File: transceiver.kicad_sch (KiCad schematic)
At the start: 82 parts, among them J2 Conn_01x04_Male, J3 Conn_01x04_Male, J4 Conn_01x04_Male, J5 Conn_01x06_Male, J6 Conn_01x05_Male, J7 Conn_01x05_Male, J8 Conn_01x05_Male, J9 Conn_01x04_Male, U10 74LVC1G3157, U11 SP330EEY-L, U12 TXS0104EDR, U13 74LVC1G3157, U14 MAX3222EIPW, U4 74LVC1G3157, U5 SP330EEY-L, U6 74LVC1G3157, U7 TLV75525PDBV, U8 TXS0104EDR, U9 TLV75518PDBV

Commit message: After update to kicak 9.0
Signed-off-by: Marc Kelly <mpkelly@achenar.co.uk>
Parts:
- C19, C20, C21, C22, C23, C24, C25, C26, C27, C28, C29, C30, C31, C32, C33, C34, C35, C36, C37, C38, C39: MFN (none) -> Kemet; MFP (none) -> C0603C104J4RACTU; SUPPLIER (none) -> Mouser; SUPPLIER_LINK (none) -> https://www.mouser.co.uk/ProductDetail/KEMET/C0603C104J4RAC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; SUPPLIER_PN (none) -> 80-C0603C104J4R
- D10, D11, D4, D5, D6, D7, D8, D9: MFN (none) -> Wurth; MFP (none) -> 155060GS75300; SUPPLIER (none) -> Mouser; SUPPLIER_LINK (none) -> https://www.mouser.co.uk/ProductDetail/Wurth-Elektronik/155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; SUPPLIER_PN (none) -> 710-155060GS75300
- J2, J3, J4, J9: MFN (none) -> Ampheonol; MFP (none) -> 68604-804HLF; SUPPLIER (none) -> Mouser; SUPPLIER_LINK (none) -> https://www.mouser.co.uk/ProductDetail/Amphenol-FCI/68604-8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; SUPPLIER_PN (none) -> 649-68604-804HLF
- J5: MFN (none) -> Ampheonol; MFP (none) -> 68024-106HLF; SUPPLIER (none) -> Mouser; SUPPLIER_LINK (none) -> https://www.mouser.co.uk/ProductDetail/Amphenol-FCI/68024-1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; SUPPLIER_PN (none) -> 649-68024-106HLF
- J6, J7, J8: MFN (none) -> Ampheonol; MFP (none) -> 68024-405HLF; SUPPLIER (none) -> Mouser; SUPPLIER_LINK (none) -> https://www.mouser.co.uk/ProductDetail/Amphenol-FCI/68024-4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; SUPPLIER_PN (none) -> 649-68024-405HLF
- JP1, JP12: MFN (none) -> Ampheonol; MFP (none) -> 57202-F52-03LF; SUPPLIER (none) -> Mouser; SUPPLIER_LINK (none) -> https://www.mouser.co.uk/ProductDetail/Amphenol-FCI/57202-F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; SUPPLIER_PN (none) -> 649-57202-F52-03LF
- JP19, JP23, JP4, JP8: MFN (none) -> Ampheonol; MFP (none) -> 57202-G52-04LF; SUPPLIER (none) -> Mouser; SUPPLIER_LINK (none) -> https://www.mouser.co.uk/ProductDetail/Amphenol-FCI/57202-G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; SUPPLIER_PN (none) -> 649-57202-G52-04LF
- JP27, JP28, JP29, JP30: MFN (none) -> Samtech; MFP (none) -> TMM-116-01-G-S-SM; Notes (none) -> Buy a strip, cut to length! get a x16; SUPPLIER (none) -> Mouser; SUPPLIER_LINK (none) -> https://www.mouser.co.uk/ProductDetail/Samtec/TMM-116-01-G-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; SUPPLIER_PN (none) -> 200-TMM11601GSSM
- R10, R11, R12, R13, R14, R9: value 4.7k -> 4k7; MFN (none) -> Generic; SUPPLIER (none) -> Mouser; SUPPLIER_PN (none) -> 603-RT0603DRE074K7L
- R15, R16, R17, R18, R19: MFN (none) -> Generic; SUPPLIER (none) -> Mouser; SUPPLIER_PN (none) -> 603-RT0603DRE074K7L
- R21, R22, R23, R24, R25, R26, R27, R28: MFN (none) -> Generic; SUPPLIER (none) -> Mouser; SUPPLIER_PN (none) -> 754-RG1608P-331-BT5
- R31, R32, R33, R34: MFN (none) -> Generic; SUPPLIER (none) -> Mouser; SUPPLIER_PN (none) -> 603-RT0603FRE07120RL
- U10, U13, U4, U6: MFN (none) -> TI; MFP (none) -> SN74LVC1G3157DBVR; SUPPLIER (none) -> Mouser; SUPPLIER_LINK (none) -> https://www.mouser.co.uk/ProductDetail/Texas-Instruments/SN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; SUPPLIER_PN (none) -> 595-SN74LVC1G3157DBV
- U11, U5: MFN (none) -> MaxLinear; MFP (none) -> SP330EEY-L; SUPPLIER (none) -> Mouser; SUPPLIER_LINK (none) -> https://www.mouser.co.uk/ProductDetail/MaxLinear/SP330EEY-L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; SUPPLIER_PN (none) -> 701-SP330EEY-L
- U12, U8: MFN (none) -> TI; MFP (none) -> TXS0104ED; SUPPLIER (none) -> Mouser; SUPPLIER_LINK (none) -> https://www.mouser.co.uk/ProductDetail/Texas-Instruments/TX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; SUPPLIER_PN (none) -> 595-TXS0104ED
- U14: MFN (none) -> TI; MFP (none) -> MAX3222ECDWR; SUPPLIER (none) -> Mouser; SUPPLIER_LINK (none) -> https://www.mouser.co.uk/ProductDetail/Texas-Instruments/MA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; SUPPLIER_PN (none) -> 595-MAX3222ECDWR
- U7: MFN (none) -> TI; MFP (none) -> TLV75525PDBVR; SUPPLIER (none) -> Mouser; SUPPLIER_LINK (none) -> https://www.mouser.co.uk/ProductDetail/Texas-Instruments/TL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; SUPPLIER_PN (none) -> 595-TLV75525PDBVR
- U9: MFN (none) -> TI; MFP (none) -> TLV75518PDBVR; SUPPLIER (none) -> Mouser; SUPPLIER_LINK (none) -> https://www.mouser.co.uk/ProductDetail/Texas-Instruments/TL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; SUPPLIER_PN (none) -> 595-TLV75518PDBVR

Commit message: Updated to remove the level shifters
Just have 3v3 ttl outputs for now, trancievers will be on different
boards
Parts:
- removed C19, C20, C21, C22, C23, C24, C25, C26, C27, C28, C29, C30, C31, C32, C33, C34, C35, C36, C37, C38, C39: 100nF, Capacitor_SMD:C_0603_1608Metric_Pad1.08x0.95mm_HandSolder, symbol Device:C_Small
- removed J2, J3, J4, J9: Conn_01x04_Male, Connector_PinHeader_2.54mm:PinHeader_1x04_P2.54mm_Vertical, symbol Connector:Conn_01x04_Male
- removed J5: Conn_01x06_Male, Connector_PinHeader_2.54mm:PinHeader_1x06_P2.54mm_Vertical, symbol Connector:Conn_01x06_Male
- removed J6, J7, J8: Conn_01x05_Male, Connector_PinHeader_2.54mm:PinHeader_1x05_P2.54mm_Vertical, symbol Connector:Conn_01x05_Male
- removed JP1, JP12: Jumper, Connector_PinHeader_2.00mm:PinHeader_2x03_P2.00mm_Vertical_SMD, symbol Connector_Generic:Conn_02x03_Odd_Even
- removed JP19, JP23, JP4, JP8: Jumper, Connector_PinHeader_2.00mm:PinHeader_2x04_P2.00mm_Vertical_SMD, symbol Connector_Generic:Conn_02x04_Odd_Even
- removed JP27, JP28, JP29, JP30: Jumper, Connector_PinHeader_2.00mm:PinHeader_1x02_P2.00mm_Vertical_SMD_Pin1Left, symbol Device:Jumper
- removed R10, R11, R12, R13, R14, R15, R18, R19, R9: 4k7, Resistor_SMD:R_0603_1608Metric_Pad0.98x0.95mm_HandSolder, symbol Device:R_Small
- removed R31, R32, R33, R34: 120R, Resistor_SMD:R_0603_1608Metric_Pad0.98x0.95mm_HandSolder, symbol Device:R_Small
- removed U10, U13, U4, U6: 74LVC1G3157, Package_TO_SOT_SMD:SOT-23-6_Handsoldering, symbol 74xGxx:74LVC1G3157
- removed U11, U5: SP330EEY-L, Package_SO:TSSOP-24_4.4x7.8mm_P0.65mm, symbol local:SP330EEY-L
- removed U12, U8: TXS0104EDR, Package_SO:SOIC-14_3.9x8.7mm_P1.27mm, symbol local:TXS0104EDR
- removed U14: MAX3222EIPW, Package_SO:SO-20_12.8x7.5mm_P1.27mm, symbol local:MAX3222EIPW
- added D1, D2, D3, D4: Y_LED, LED_SMD:LED_0603_1608Metric_Pad1.05x0.95mm_HandSolder, symbol Device:LED
- added D18, D19, D20, D21: ESDS304, Package_TO_SOT_SMD:SOT-23-5, symbol Power_Protection:ESDS304
- added J1, J2, J3, J4: Conn_02x06_Odd_Even, symbol Connector_Generic:Conn_02x06_Odd_Even
- added R1, R2, R3, R4: 330R, Resistor_SMD:R_0603_1608Metric_Pad0.98x0.95mm_HandSolder, symbol Device:R_Small
- renumbered D9 to D10, D10 to D11, D11 to D12, D4 to D5, D5 to D6, D6 to D7, D7 to D8, D8 to D9, JP15 to JP1, R26 to R10, R27 to R11, R28 to R12, R16 to R13, R17 to R14, R21 to R5, R22 to R6, R23 to R7, R24 to R8, R25 to R9, U7 to U1, U9 to U2
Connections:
- net BDBUS0 is gone; now on net ADBUS0: R5.2
- net BDBUS1 is gone; now on net ADBUS1: R6.2
- net CDBUS0 is gone; now on net ADBUS0: R7.2
- net CDBUS1 is gone; now on net ADBUS1: R8.2
- net DDBUS0 is gone; now on net ADBUS0: R11.2
- net DDBUS1 is gone; now on net ADBUS1: R12.2
- net Vdrive is gone; now on net GND: JP1.2 (Pin_2), JP1.4 (Pin_4), JP1.6 (Pin_6), JP1.8 (Pin_8)
- net +3V3: no longer JP1.5 (Pin_5)
- net ADBUS0: now also D18.1 (K), J1.1 (Pin_1), J2.1 (Pin_1), J3.1 (Pin_1), J4.1 (Pin_1)
- net ADBUS1: now also D18.3 (K), J1.2 (Pin_2), J2.2 (Pin_2), J3.2 (Pin_2), J4.2 (Pin_2)
- net ADBUS2: now also D18.4 (K), J1.3 (Pin_3), J2.3 (Pin_3), J3.3 (Pin_3), J4.3 (Pin_3)
- net ADBUS3: now also D18.5 (K), J1.4 (Pin_4), J2.4 (Pin_4), J3.4 (Pin_4), J4.4 (Pin_4)
- net ADBUS4: now also J1.5 (Pin_5), J2.5 (Pin_5), J3.5 (Pin_5), J4.5 (Pin_5)
- net ADBUS7: now also J1.6 (Pin_6), J2.6 (Pin_6), J3.6 (Pin_6), J4.6 (Pin_6)
- net CTSn_2: now also D19.5 (K)
- net CTSn_3: now also D20.5 (K)
- net CTSn_4: now also D21.5 (K)
- net GND: now also D18.2 (A), D19.2 (A), D20.2 (A), D21.2 (A), J1.7 (Pin_7), J1.8 (Pin_8), J2.7 (Pin_7), J2.8 (Pin_8), J3.7 (Pin_7), J3.8 (Pin_8), J4.7 (Pin_7), J4.8 (Pin_8)
- net RTSn_2: now also D19.4 (K)
- net RTSn_3: now also D20.4 (K)
- net RTSn_4: now also D21.4 (K)
- net RXD_2: now also D19.3 (K)
- net RXD_3: now also D20.3 (K)
- net RXD_4: now also D21.3 (K)
- net TXD_2: now also D19.1 (K)
- net TXD_3: now also D20.1 (K)
- net TXD_4: now also D21.1 (K)
- net VBUS: now also J1.9 (Pin_9), J2.9 (Pin_9), J3.9 (Pin_9), J4.9 (Pin_9), R1.2
- new net: D1.2 (A), R1.1
- new net: D2.2 (A), R2.1
- new net: D4.2 (A), R4.1
- new net: D3.2 (A), R3.1
- new net 1V8: J1.11 (Pin_11), J2.11 (Pin_11), J3.11 (Pin_11), J4.11 (Pin_11), R4.2
- new net 2V5: J1.10 (Pin_10), J2.10 (Pin_10), J3.10 (Pin_10), J4.10 (Pin_10), R3.2
- new net 3V3: J1.12 (Pin_12), J2.12 (Pin_12), J3.12 (Pin_12), J4.12 (Pin_12), R2.2
- new net 3v3: JP1.5 (Pin_5)
- no-connect marks 14 -> 8
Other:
- note added: "Mapping of Busto Serial 0: TXD 1: RXD 2: RTSn 3: CTSn 4: DTRn 5: DSRn 6: DCDn 7: TXDEN"
- note added: "Ouput Connector 2x6 (10 pin) 1: TXD 2: RXD 3: RTSn 4: CTSn 5: DTRn 6: TXDEN 7: GND 8; GND 9: 5v0 10: 2v5 11: 1v8 12: 3v3"
- note added: "Power Test Point and LEDS"
- note added: "We should use shottkey protection clamps 2x8 arrays maybe"
- note removed: "1.27mm 2pin headers - Disconnect XCVR"
- note removed: "2mm 2pin headers - Disconnect XCVR"
- note removed: "BUSA: CMOS/TTL BUSB: RS232 BUSC: RS422/485/RS232 BUSC: RS422/485/RS232"
- note removed: "Convert the 3v3 Logic to 1v8, then we can do 1v8 to ANY upto 5V on the second stage."
- note removed: "Gives direct TTL access"
- note removed: "Gives direct TTL access 3v3 bypassing level shifters"
- note removed: "Mapping of Bus to Serial 0: TXD 1: RXD 2: RTSn 3: CTSn 4: DTRn 5: DSRn 6: DCDn 7: TXDEN"
- note removed: "Maybe some screw terminals?"
- note removed: "Port 2 - RS232"
- note removed: "Port 3 - RS422/485/RS232"
- note removed: "Port 4 - RS422/485/RS232"
- note removed: "Termination resistors for the rs485 Ports 3 & 4"
- moved on the sheet: D10, D11, D12, D5, D6, D7, D8, D9, JP1, R10, R11, R12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

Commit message: Updated power leds and external protection on Serial
Signed-off-by: Marc Kelly <mpkelly@achenar.co.uk>
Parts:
- removed D3: Y_LED, LED_SMD:LED_0603_1608Metric_Pad1.05x0.95mm_HandSolder, symbol Device:LED
- removed R3: 330R, Resistor_SMD:R_0603_1608Metric_Pad0.98x0.95mm_HandSolder, symbol Device:R_Small
- added D2, D4: ESDS304, Package_TO_SOT_SMD:SOT-23-5, symbol Power_Protection:ESDS304
- added D8: Y_LED, LED_SMD:LED_0603_1608Metric_Pad1.05x0.95mm_HandSolder, symbol Device:LED
- added Q1, Q2: SI500N025UK-TP, Package_TO_SOT_SMD:SOT-23, symbol Transistor_FET:Q_NMOS_GSD
- added R2, R5, R6: 330R, Resistor_SMD:R_0603_1608Metric_Pad0.98x0.95mm_HandSolder, symbol Device:R_Small
- J1, J2, J3, J4: footprint (none) -> Connector_PinSocket_2.54mm:PinSocket_2x06_P2.54mm_Horizontal
- renumbered D18 to D1, D2 to D10, D5 to D11, D6 to D12, D7 to D13, D8 to D14, D9 to D15, D10 to D16, D11 to D17, D12 to D18, D19 to D3, D20 to D5, D21 to D6, D4 to D7, D1 to D9, R4 to R1, R8 to R10, R9 to R11, R10 to R12, R11 to R13, R12 to R14, R13 to R15, R14 to R16, R1 to R3, R2 to R4, R5 to R7, R6 to R8, R7 to R9
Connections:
- net 1V8: no longer R1.2
- net 3v3: now also R1.2, R2.2
- net ADBUS0: no longer J2.1 (Pin_1), J3.1 (Pin_1), J4.1 (Pin_1), R13.2, R7.2, R9.2
- net ADBUS1: no longer J2.2 (Pin_2), J3.2 (Pin_2), J4.2 (Pin_2), R10.2, R14.2, R8.2
- net ADBUS2: no longer J2.3 (Pin_3), J3.3 (Pin_3), J4.3 (Pin_3)
- net ADBUS3: no longer J2.4 (Pin_4), J3.4 (Pin_4), J4.4 (Pin_4)
- net ADBUS4: now also D2.5 (K); no longer J2.5 (Pin_5), J3.5 (Pin_5), J4.5 (Pin_5)
- net ADBUS7: now also D2.4 (K); no longer J2.6 (Pin_6), J3.6 (Pin_6), J4.6 (Pin_6)
- net CTSn_4: now also J4.4 (Pin_4)
- net GND: now also D10.1 (K), D9.1 (K), D2.2 (A), D4.2 (A), Q1.2 (S), Q2.2 (S)
- net at D7.1 (K): now also Q1.3 (D)
- net CTSn_2 renamed BDBUS3
- net BDBUS3: now also J2.4 (Pin_4)
- net CTSn_3 renamed CDBUS3
- net CDBUS3: now also J3.4 (Pin_4)
- net RTSn_2 renamed BDBUS2
- net BDBUS2: now also J2.3 (Pin_3)
- net RTSn_3 renamed CDBUS2
- net CDBUS2: now also J3.3 (Pin_3)
- net RTSn_4 renamed DDBUS2
- net DDBUS2: now also J4.3 (Pin_3)
- net RXD_2 renamed BDBUS1
- net BDBUS1: now also J2.2 (Pin_2), R8.2
- net RXD_3 renamed CDBUS1
- net CDBUS1: now also J3.2 (Pin_2), R10.2
- net RXD_4 renamed DDBUS1
- net DDBUS1: now also J4.2 (Pin_2), R14.2
- net TXD_2 renamed BDBUS0
- net BDBUS0: now also J2.1 (Pin_1), R7.2
- net TXD_3 renamed CDBUS0
- net CDBUS0: now also J3.1 (Pin_1), R9.2
- net TXD_4 renamed DDBUS0
- net DDBUS0: now also J4.1 (Pin_1), R13.2
- new net: Q1.1 (G), R5.2
- new net: Q2.1 (G), R6.2
- new net: D8.1 (K), Q2.3 (D)
- new net: D8.2 (A), R2.1
- new net 1v8: R6.1
- new net 2v5: R5.1
- new net BDBUS4: D2.3 (K), J2.5 (Pin_5)
- new net BDBUS7: D2.1 (K), J2.6 (Pin_6)
- new net CDBUS4: D4.5 (K), J3.5 (Pin_5)
- new net CDBUS7: D4.4 (K), J3.6 (Pin_6)
- new net DDBUS4: D4.3 (K), J4.5 (Pin_5)
- new net DDBUS7: D4.1 (K), J4.6 (Pin_6)
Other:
- note added: "These are NPN driven due to low supply voltages"
- note removed: "Need to generate 2v5 and 1v8 from 3v3 3v3 and 5v are used as is. OR an external voltage can be used. If no pins are jumpered, then external is the ref."
- moved on the sheet: D10, D7, D9, JP1, R1, R3, R4, U1, U2

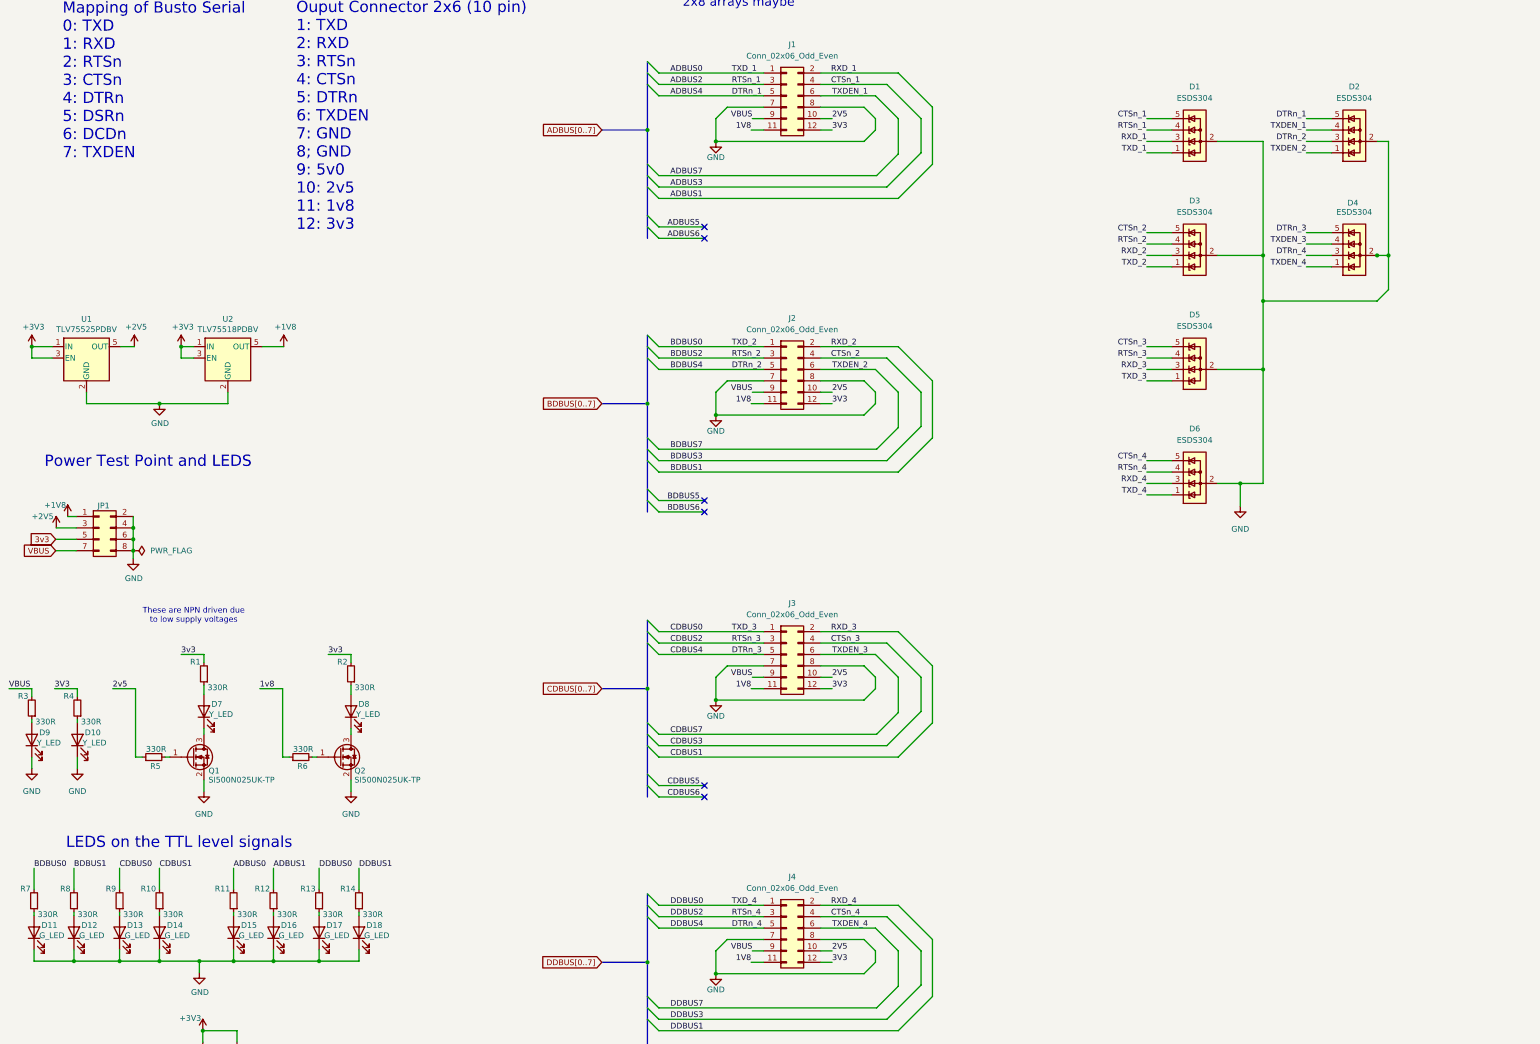
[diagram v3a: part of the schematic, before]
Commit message: Updated with the new design.
Removed all level translators.
4 sockets, 2x6 pin outputs
New PCB shape and routing
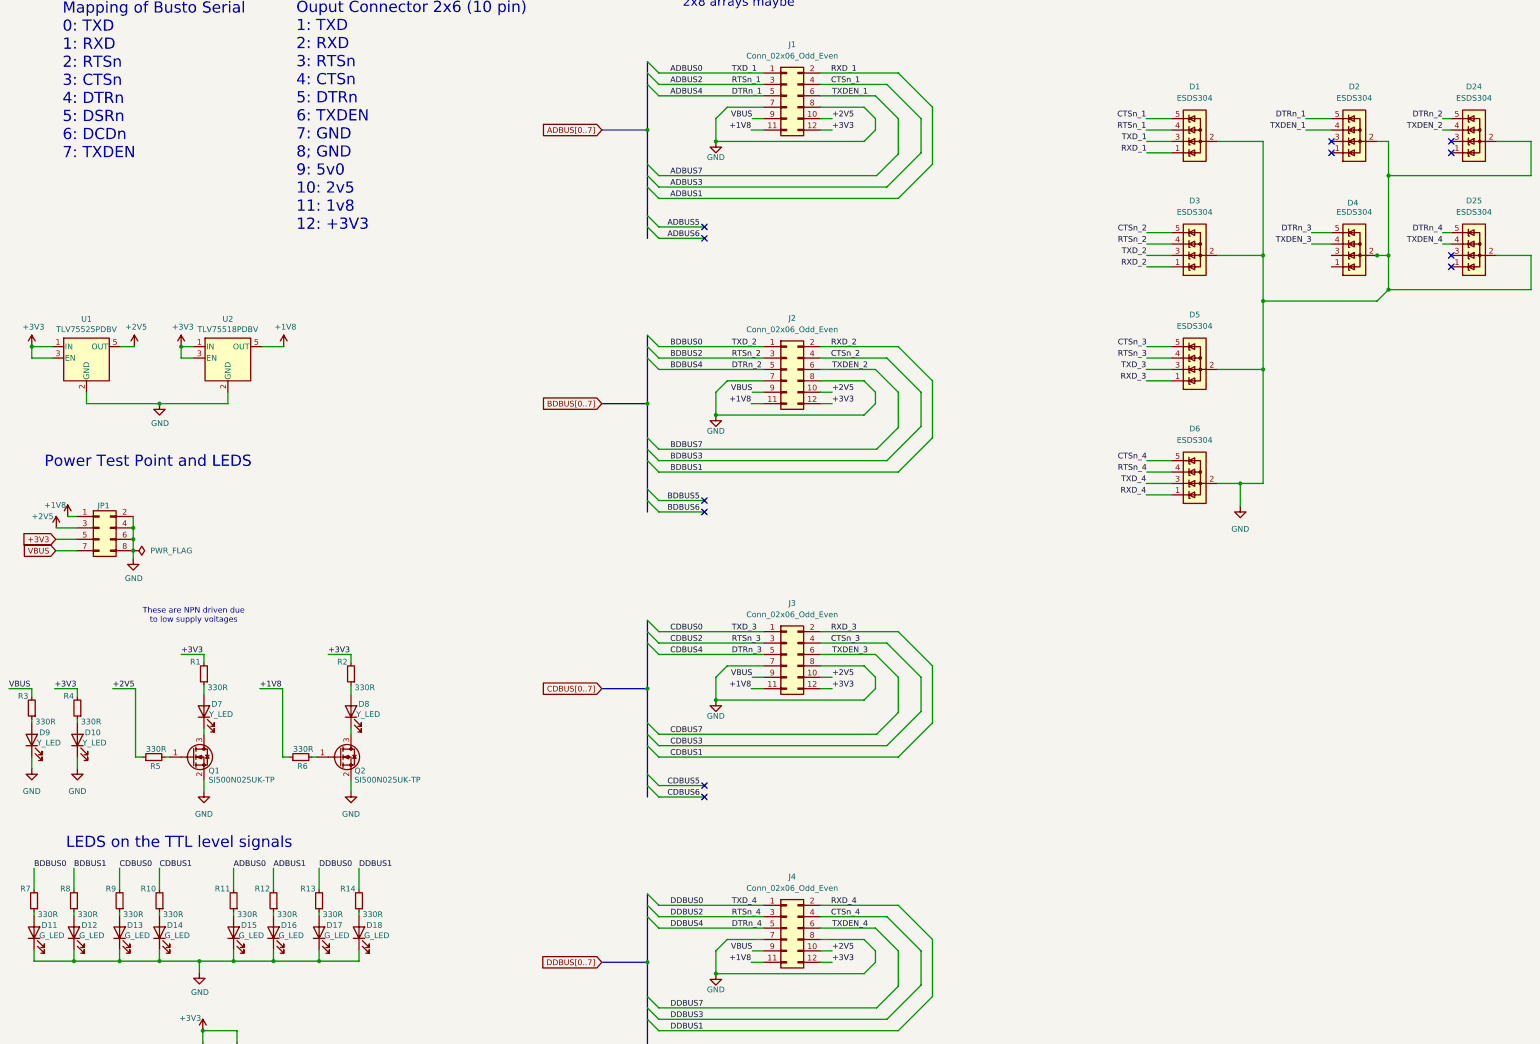
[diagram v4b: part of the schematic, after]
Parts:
- added D24, D25: ESDS304, Package_TO_SOT_SMD:SOT-23-5, symbol Power_Protection:ESDS304
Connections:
- net 1V8 is gone; now on net +1V8: J1.11 (Pin_11), J2.11 (Pin_11), J3.11 (Pin_11), J4.11 (Pin_11)
- net 1v8 is gone; now on net +1V8: R6.1
- net 2V5 is gone; now on net +2V5: J1.10 (Pin_10), J2.10 (Pin_10), J3.10 (Pin_10), J4.10 (Pin_10)
- net 2v5 is gone; now on net +2V5: R5.1
- net 3V3 is gone; now on net +3V3: J1.12 (Pin_12), J2.12 (Pin_12), J3.12 (Pin_12), J4.12 (Pin_12), R4.2
- net 3v3 is gone; now on net +3V3: JP1.5 (Pin_5), R1.2, R2.2
- net ADBUS0: now also D1.3 (K); no longer D1.1 (K)
- net ADBUS1: now also D1.1 (K); no longer D1.3 (K)
- net BDBUS0: now also D3.3 (K); no longer D3.1 (K)
- net BDBUS1: now also D3.1 (K); no longer D3.3 (K)
- net BDBUS4: now also D24.5 (K); no longer D2.3 (K)
- net BDBUS7: now also D24.4 (K); no longer D2.1 (K)
- net CDBUS0: now also D5.3 (K); no longer D5.1 (K)
- net CDBUS1: now also D5.1 (K); no longer D5.3 (K)
- net DDBUS0: now also D6.3 (K); no longer D6.1 (K)
- net DDBUS1: now also D6.1 (K); no longer D6.3 (K)
- net DDBUS4: now also D25.5 (K); no longer D4.3 (K)
- net DDBUS7: now also D25.4 (K); no longer D4.1 (K)
- net GND: now also D24.2 (A), D25.2 (A)
- no-connect marks 8 -> 14
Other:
- note added: "Ouput Connector 2x6 (10 pin) 1: TXD 2: RXD 3: RTSn 4: CTSn 5: DTRn 6: TXDEN 7: GND 8; GND 9: 5v0 10: 2v5 11: 1v8 12: +3V3"
- note removed: "Ouput Connector 2x6 (10 pin) 1: TXD 2: RXD 3: RTSn 4: CTSn 5: DTRn 6: TXDEN 7: GND 8; GND 9: 5v0 10: 2v5 11: 1v8 12: 3v3"

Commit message: Sorting out BOMs
Signed-off-by: Marc Kelly <mpkelly@achenar.co.uk>
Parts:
- D1, D2, D24, D25, D3, D4, D5, D6: MFN (none) -> Texas Instruments; MFP (none) -> ESDS304DBVR; SUPPLIER (none) -> Mouser; SUPPLIER_PN (none) -> 595-ESDS304DBVR
- J1, J2, J3, J4: MFN (none) -> Amphenol FCI; MFP (none) -> 10129382-912003BLF; SUPPLIER (none) -> Mouser; SUPPLIER_PN (none) -> 649-1012938291203BLF
- JP1: MFN (none) -> Amphenol FCI; MFP (none) -> 20021121-00008D4LF; SUPPLIER (none) -> Mouser; SUPPLIER_PN (none) -> 649-221121-00008D4LF
- Q1, Q2: value SI500N025UK-TP -> FDV301N; MFN (none) -> OnSemi; MFP (none) -> FDV301N; SUPPLIER (none) -> Mouser; SUPPLIER_PN (none) -> 512-FDV301N
- R15, R16: MFP (none) -> 4.7k 1%
